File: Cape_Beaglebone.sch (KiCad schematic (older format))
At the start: 91 parts, among them IC1 MPU-9250, IC10 HMC5883L-TR, IC11 BMP180, IC12 ADS8688IDBT, IC13 L3GD20H, IC2 HX711, IC3 DS3231S, IC4 HX711, IC5 CAT24C256WI-GT3, IC6 AD7793BRUZ, IC7 AD7793BRUZ, IC8 MPU-6500, IC9 LSM303D, J1 Conn_01x04, J10 Conn_01x04, J11 Conn_01x06, J12 Conn_01x04, J13 Conn_01x04, J14 Conn_01x04, J15 Conn_01x04, J16 Conn_01x06, J2 Conn_01x04, J3 Conn_01x02, J4 Conn_01x06, J5 M_WP, J6 Conn_01x06, J7 Conn_01x04, J8 Conn_01x04, J9 Conn_01x04, P1 BeagleBone_Black_Header, P2 BeagleBone_Black_Header, Q1 BC807, Q2 BC807, SW1 SW_DIP_x02, U1 4525DO-DS5AI001DP

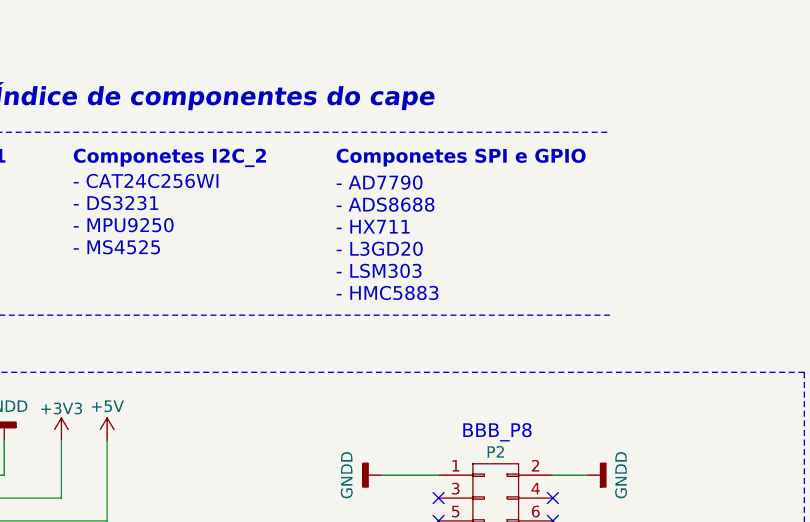
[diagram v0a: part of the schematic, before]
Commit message: Corte para mangeira
Alteração para facilitar a colocação de magueira no sensor de pressão
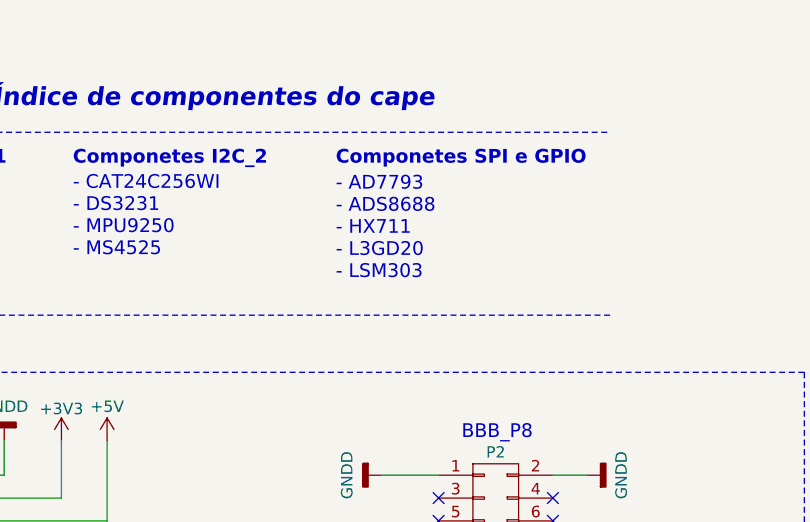
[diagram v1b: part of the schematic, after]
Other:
- note added: "- AD7793\n- ADS8688\n- HX711\n- L3GD20\n- LSM303"
- note removed: "- AD7790\n- ADS8688\n- HX711\n- L3GD20\n- LSM303\n- HMC5883"
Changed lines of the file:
@@
 Text Notes 3650 1250 0    60   ~ 12
 Componetes SPI e GPIO
-Text Notes 3650 1850 0    60   ~ 0
-- AD7790\n- ADS8688\n- HX711\n- L3GD20\n- LSM303\n- HMC5883
+Text Notes 3650 1750 0    60   ~ 0
+- AD7793\n- ADS8688\n- HX711\n- L3GD20\n- LSM303
 Text Notes 2150 1000 0    79   Italic 16
 Índice de componentes do cape

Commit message: Atualizando para Kicad 5.1.0
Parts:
- C1, C10, C11, C12, C13, C14, C15, C16, C17, C18, C19, C2, C20, C21, C22, C23, C24, C25, C26, C27, C28, C29, C3, C30, C31, C32, C33, C34, C4, C5, C6, C7, C8: symbol device:C -> Cape_Beaglebone-rescue:C-device
- J1, J10, J12, J13, J14, J15, J2, J7, J8, J9: symbol conn:Conn_01x04 -> Cape_Beaglebone-rescue:Conn_01x04-conn
- J11, J16, J4, J6: symbol conn:Conn_01x06 -> Cape_Beaglebone-rescue:Conn_01x06-conn
- J3: symbol conn:Conn_01x02 -> Cape_Beaglebone-rescue:Conn_01x02-conn
- J5: symbol conn:TEST_1P -> Cape_Beaglebone-rescue:TEST_1P-conn
- NT1, NT2: symbol device:Net-Tie_2 -> Cape_Beaglebone-rescue:Net-Tie_2-device
- Q1, Q2: symbol transistors:BC807 -> Cape_Beaglebone-rescue:BC807-transistors
- R1, R10, R11, R12, R13, R14, R15, R16, R17, R18, R2, R3, R4, R5, R6, R7, R8, R9: symbol device:R -> Cape_Beaglebone-rescue:R-device

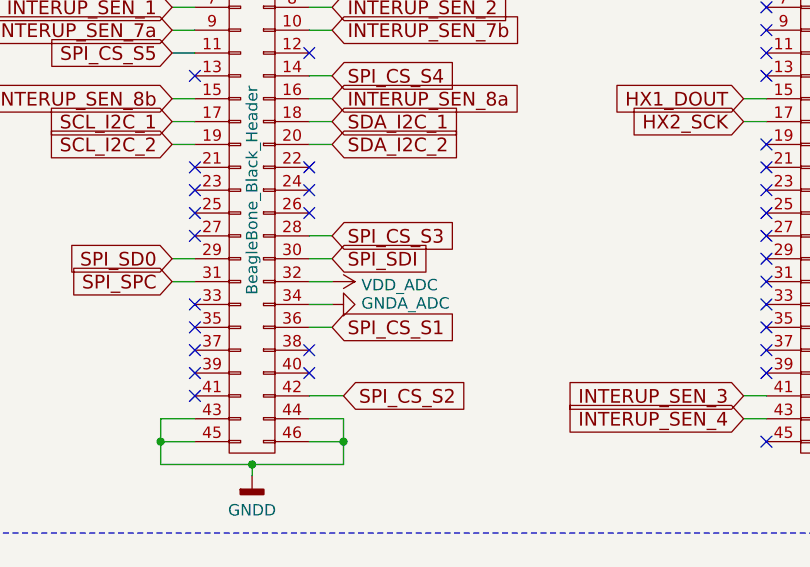
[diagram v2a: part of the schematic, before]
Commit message: Corrigi erro alias inexistente para VDD_ADC.
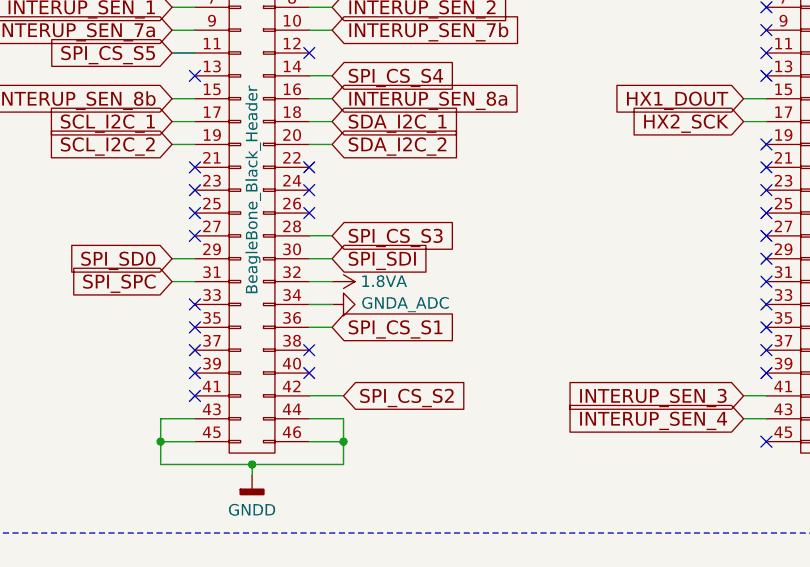
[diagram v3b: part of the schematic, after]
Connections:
- net VDD_ADC renamed 1.8VA
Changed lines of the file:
@@
 	14600 3850 14600 3950
-$Comp
-L Cape_Beaglebone-rescue:VDD_ADC #PWR0122
-U 1 1 5CA04388
-P 2200 4100
-F 0 "#PWR0122" H 2200 3950 50  0001 C CNN
-F 1 "VDD_ADC" V 2215 4228 50  0000 L CNN
-F 2 "" H 2200 4100 60  0000 C CNN
-F 3 "" H 2200 4100 60  0000 C CNN
-	1    2200 4100
-	0    1    1    0
-$EndComp
 $Comp
 L Cape_Beaglebone-rescue:GNDA_ADC #PWR0123
@@
 Wire Wire Line
 	2100 3300 2200 3300
+$Comp
+L project-power:1.8VA #PWR?
+U 1 1 5CD0C051
+P 2200 4100
+F 0 "#PWR?" H 2200 3950 50  0001 C CNN
+F 1 "1.8VA" V 2200 4225 50  0000 L CNN
+F 2 "" H 2200 4100 50  0001 C CNN
+F 3 "" H 2200 4100 50  0001 C CNN
+	1    2200 4100
+	0    1    1    0
+$EndComp
 $EndSCHEMATC
